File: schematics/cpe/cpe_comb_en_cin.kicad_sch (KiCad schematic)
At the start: 13 parts

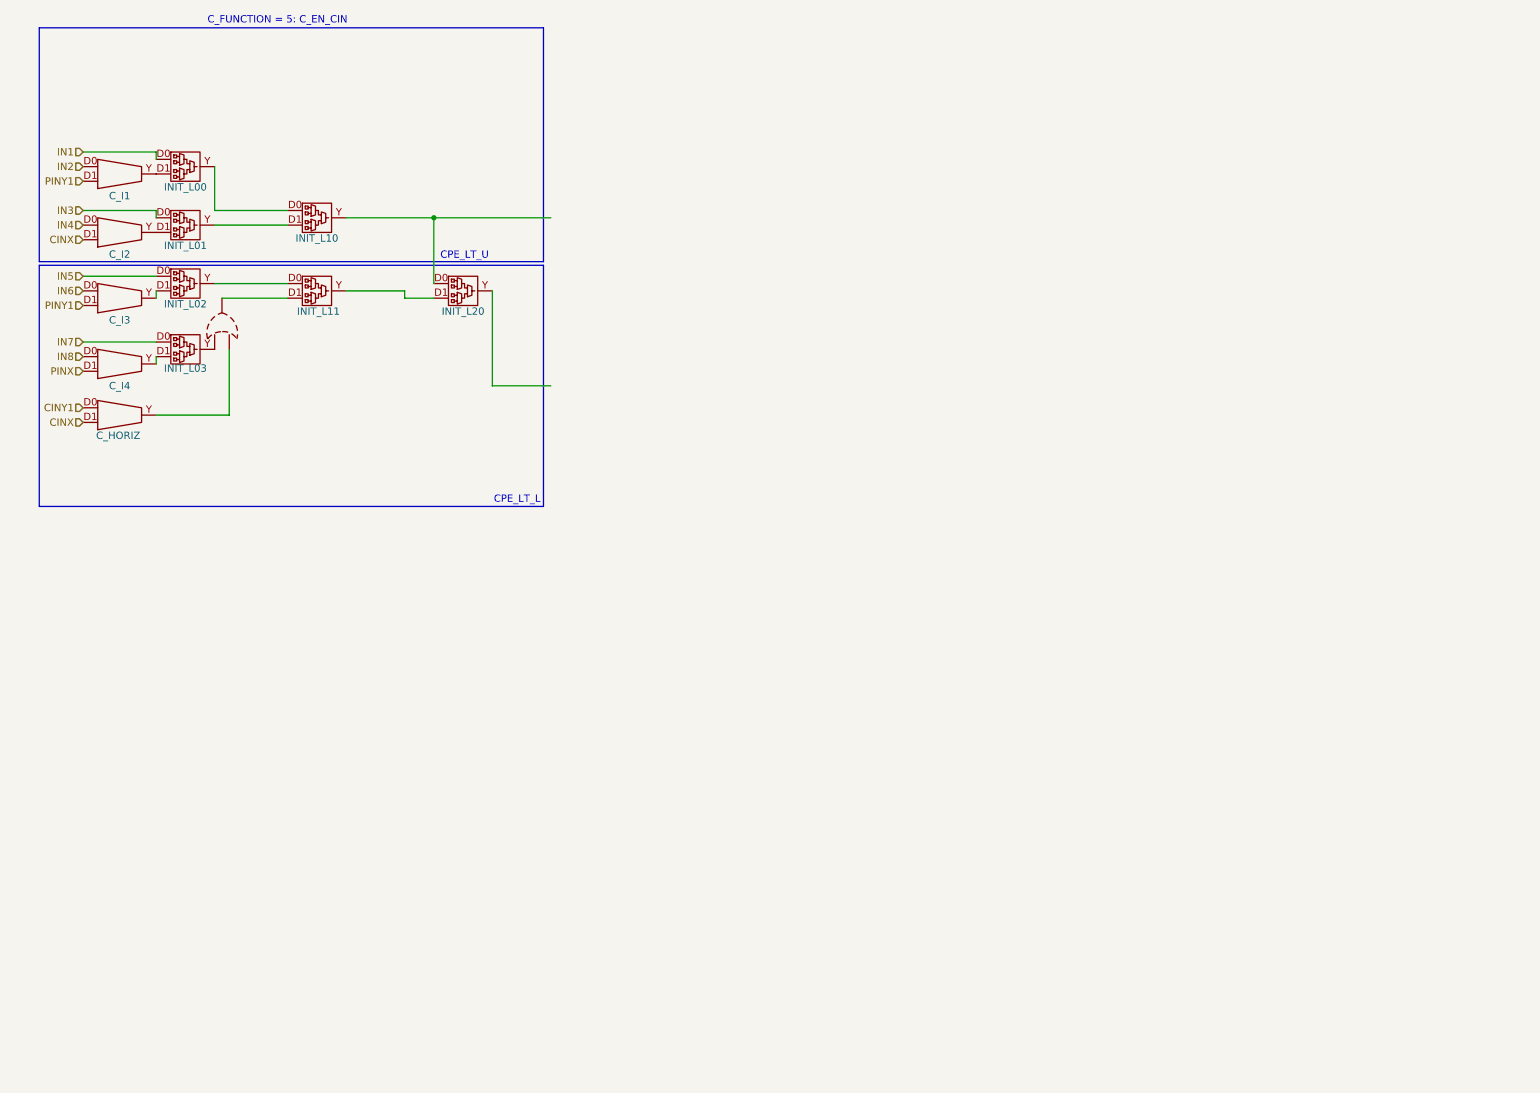
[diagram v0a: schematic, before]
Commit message: further CPE schematic updates
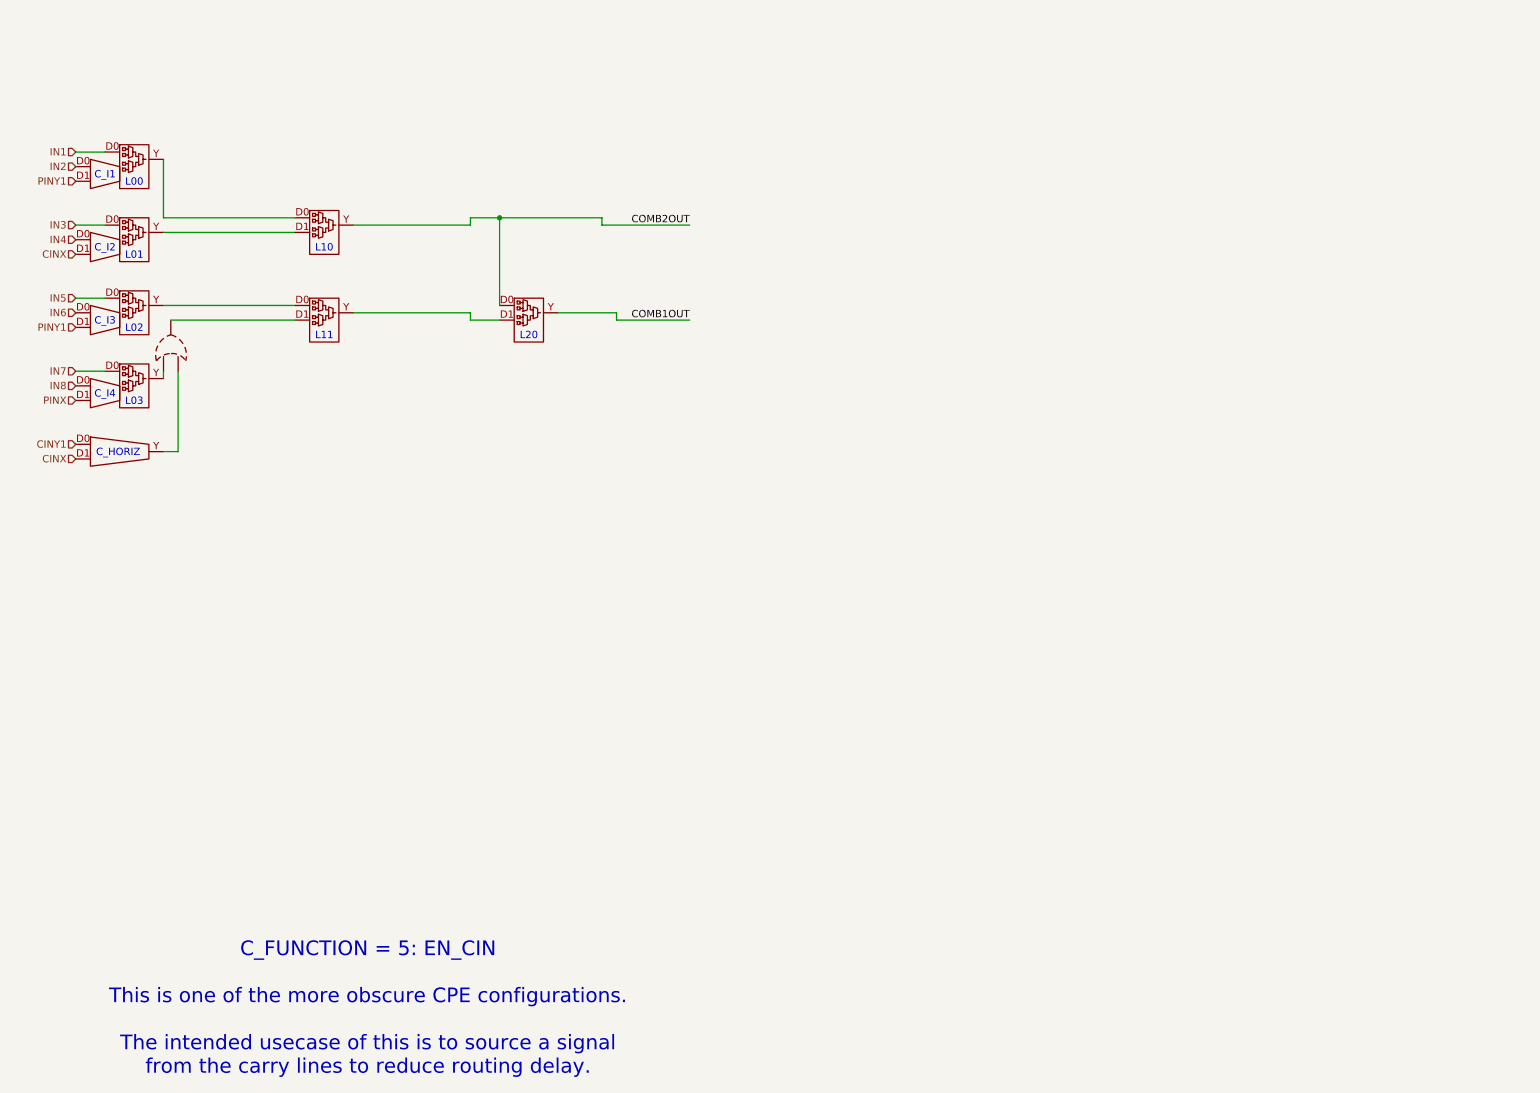
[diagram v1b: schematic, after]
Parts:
- removed C_HORIZ, C_I1, C_I2, C_I3, C_I4: ~, symbol peppercorn:MUX2B
- removed INIT_L00, INIT_L01, INIT_L02, INIT_L03, INIT_L10, INIT_L11, INIT_L20: ~, symbol peppercorn:LUT2
- removed U9: ~, symbol peppercorn:OR
- added C7: ~, symbol peppercorn:MUX2B
- added INIT_L10, INIT_L11, INIT_L18, L24: ~, symbol peppercorn:LUT2 with C_I mux
- added L25, L26, L27: ~, symbol peppercorn:LUT2
- added U41: ~, symbol peppercorn:OR
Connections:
- net CINX: now also C7.D1, INIT_L10.D1
- net CINY1: now also C7.D0
- net IN1: now also L24.D0
- net IN2: now also L24.D0
- net IN3: now also INIT_L10.D0
- net IN4: now also INIT_L10.D0
- net IN5: now also INIT_L11.D0
- net IN6: now also INIT_L11.D0
- net IN7: now also INIT_L18.D0
- net IN8: now also INIT_L18.D0
- net PINX: now also INIT_L18.D1
- net PINY1: now also INIT_L11.D1, L24.D1
- new net: L24.Y, L25.D0
- new net: INIT_L10.Y, L25.D1
- new net: C7.Y, U41.
- new net: INIT_L18.Y, U41.
- new net: L26.D1, U41.
- new net: INIT_L11.Y, L26.D0
- new net: L26.Y, L27.D1
- new net COMB1OUT: L27.Y
- new net COMB2OUT: L25.Y, L27.D0
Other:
- note added: "C_FUNCTION = 5: EN_CIN This is one of the more obscure CPE configurations. The intended usecase of this is to source a signal from the carry lines to reduce routing delay."
- note added: "C_HORIZ"
- note added: "C_I1"
- note added: "C_I2"
- note added: "C_I3"
- note added: "C_I4"
- note added: "L00"
- note added: "L01"
- note added: "L02"
- note added: "L03"
- note added: "L10"
- note added: "L11"
- note added: "L20"
- note removed: "CPE_LT_L"
- note removed: "CPE_LT_U"
- note removed: "C_FUNCTION = 5: C_EN_CIN"
- title: (none) -> CPE: Sum Input With Carry

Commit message: update schematics to include switchboxes
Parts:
- renumbered U41 to U1979
